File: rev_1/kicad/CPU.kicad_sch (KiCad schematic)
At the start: 44 parts, among them J1 Conn_01x08, J2 Conn_01x03_Pin, SW1 SW_Push, U7 STM32F303CBTx, U8 ATA6560-GAQW-N, Y1 8 MHz

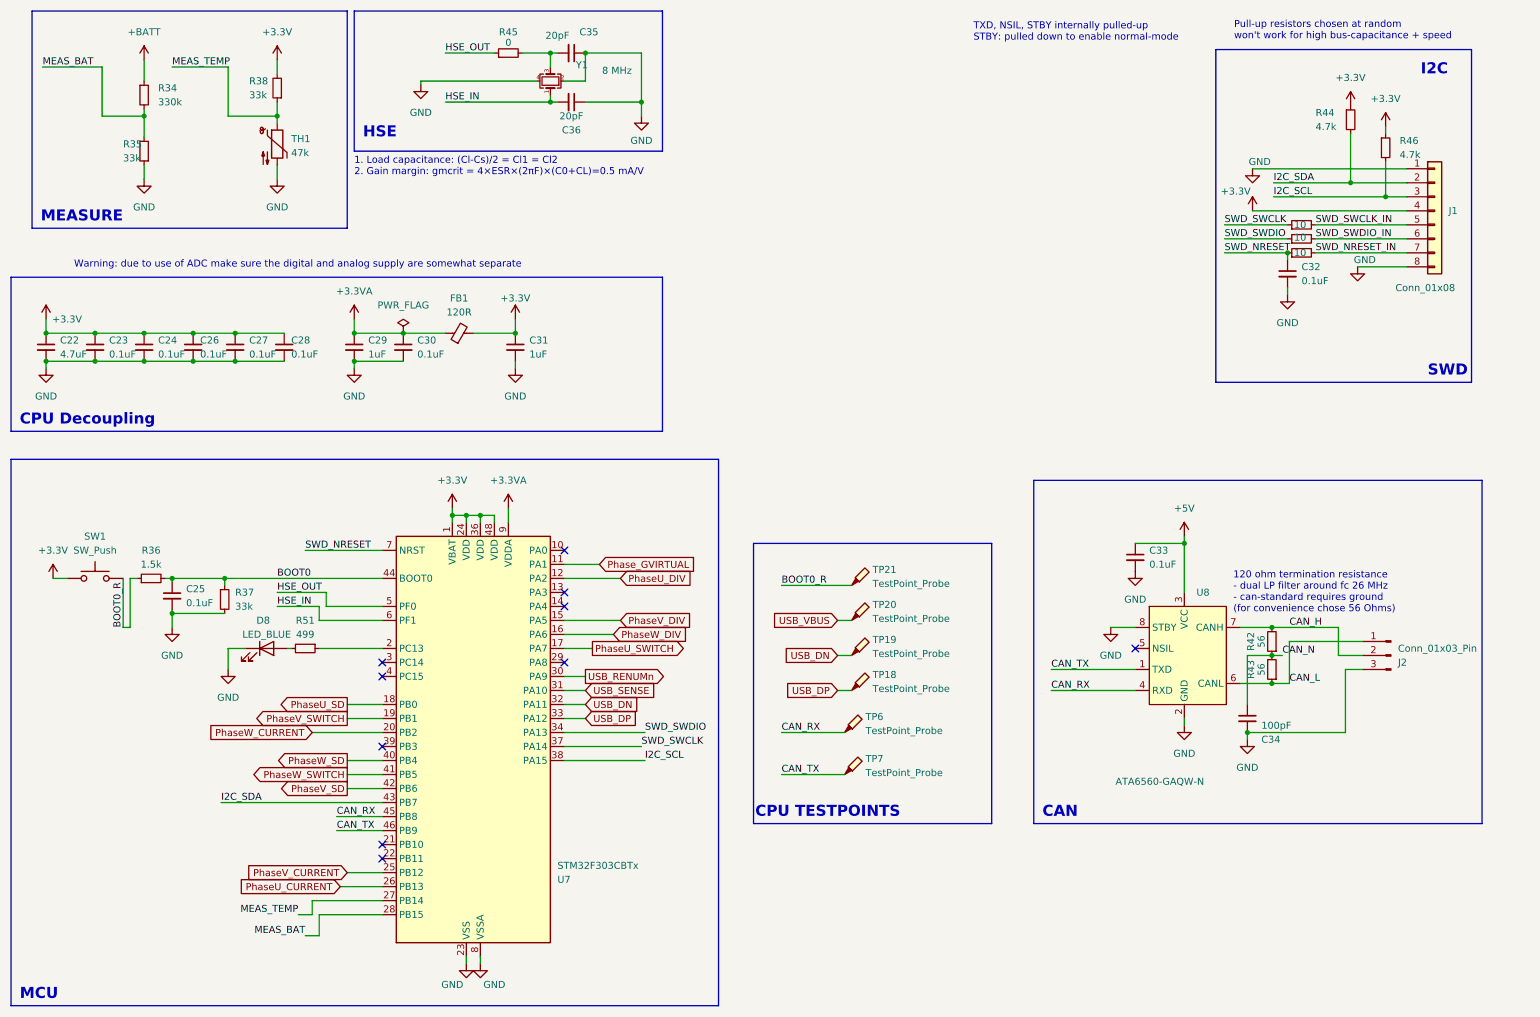
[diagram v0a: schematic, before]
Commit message: [kicad] (minor) Added comments about bldc strategy
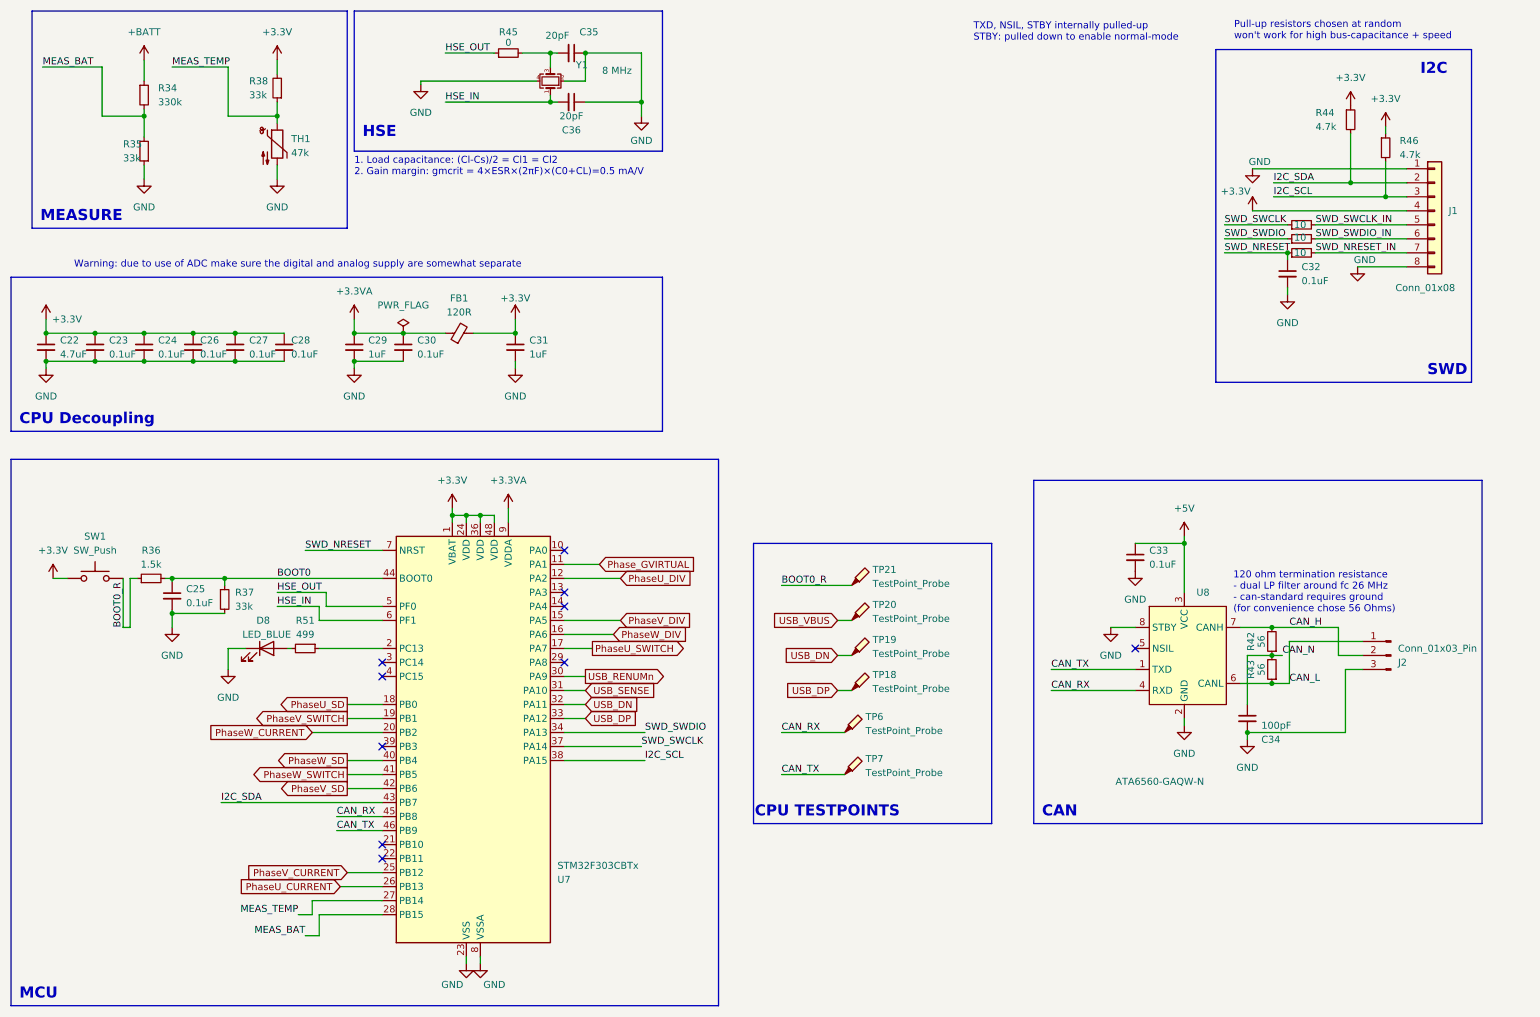
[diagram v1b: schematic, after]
